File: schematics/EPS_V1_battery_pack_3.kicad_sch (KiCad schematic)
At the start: 31 parts, among them U10 MP2672AGD-0000-Z, U11 MAX17205G+

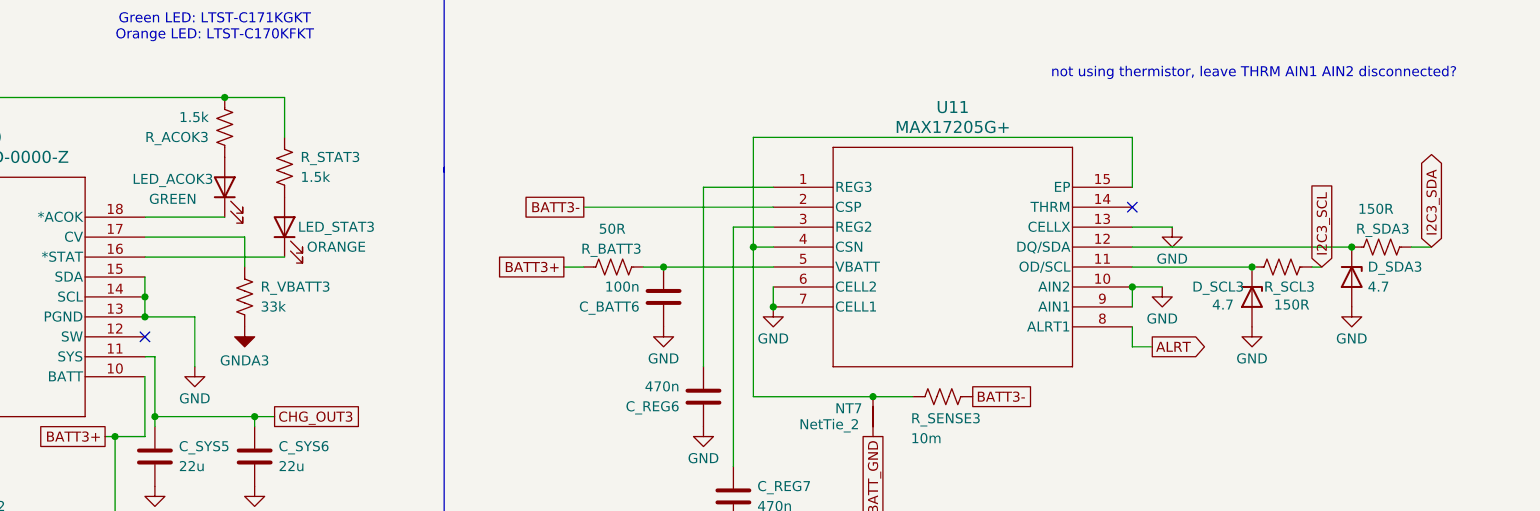
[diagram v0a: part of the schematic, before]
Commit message: Add chargers to I2C, chg_in for ADC
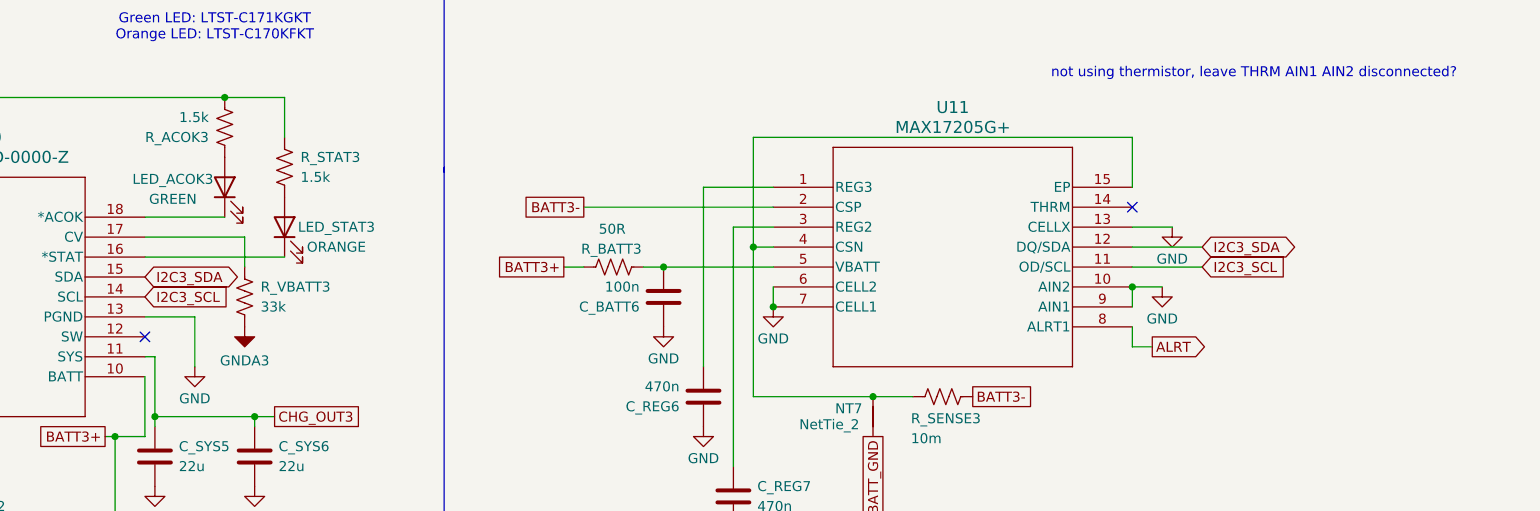
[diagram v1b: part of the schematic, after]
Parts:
- removed D_SCL3, D_SDA3: 4.7, Diode_SMD:D_0603_1608Metric, symbol Device:D_Zener
- removed R_SCL3, R_SDA3: 150R, Resistor_SMD:R_0603_1608Metric, symbol Device:R_US
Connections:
- net GND: no longer U10.14 (SCL), U10.15 (SDA)
- net I2C3_SCL: now also U10.14 (SCL), U11.11 (OD/SCL)
- net I2C3_SDA: now also U10.15 (SDA), U11.12 (DQ/SDA)

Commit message: Fix standalone to host control mode
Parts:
- removed R_VBATT3: 33k, Resistor_SMD:R_0603_1608Metric, symbol Device:R_US
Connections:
- net at C_VCC3.2, R_ACOK3.2, R_STAT3.1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: now also U10.17 (CV)
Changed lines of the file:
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@@
+	)
+	(junction
+		(at 105.41 63.5)
+		(diameter 0)
+		(color 0 0 0 0)
 	)
 	(junction
@@
 		)
 	)
-	(wire
-		(pts
-			(xy 104.14 81.28) (xy 116.84 81.28)
-		)
-		(stroke
-			(width 0)
-			(type default)
-		)
-	)
 	(polyline
 		(pts
@@
 	(wire
 		(pts
-			(xy 114.3 63.5) (xy 48.26 63.5)
+			(xy 104.14 81.28) (xy 105.41 81.28)
+		)
+		(stroke
+			(width 0)
+			(type default)
+		)
+	)
+	(wire
+		(pts
+			(xy 114.3 63.5) (xy 105.41 63.5)
 		)
 		(stroke
@@
 	(wire
 		(pts
+			(xy 105.41 81.28) (xy 105.41 63.5)
+		)
+		(stroke
+			(width 0)
+			(type default)
+		)
+	)
+	(wire
+		(pts
+			(xy 105.41 63.5) (xy 48.26 63.5)
+		)
+		(stroke
+			(width 0)
+			(type default)
+		)
+	)
+	(wire
+		(pts
 			(xy 45.72 91.44) (xy 45.72 106.68)
 		)
@@
 		(pts
 			(xy 104.14 106.68) (xy 104.14 99.06)
-		)
-		(stroke
-			(width 0)
-			(type default)
-		)
-	)
-	(wire
-		(pts
-			(xy 116.84 81.28) (xy 116.84 85.09)
 		)
 		(stroke
@@
 				(path "/85157432-5d03-48fa-ab40-27ed3d133f47/eb164b0c-5007-4f8f-b822-af0e1d9e197d"
 					(reference "#PWR0101")
-					(unit 1)
-				)
-			)
-		)
-	)
-	(symbol
-		(lib_id "sym_lib:GNDA3")
-		(at 116.84 92.71 0)
-		(unit 1)
-		(body_style 1)
-		(exclude_from_sim no)
-		(in_bom yes)
-		(on_board yes)
-		(in_pos_files yes)
-		(dnp no)
-		(property "Reference" "#PWR075"
-			(at 116.84 92.71 0)
-			(hide yes)
-			(show_name no)
-			(do_not_autoplace no)
-			(effects
-				(font
-					(size 1.27 1.27)
-				)
-			)
-		)
-		(property "Value" "GNDA3"
-			(at 116.84 97.028 0)
-			(show_name no)
-			(do_not_autoplace no)
-			(effects
-				(font
-					(size 1.27 1.27)
-				)
-			)
-		)
-		(property "Footprint" ""
-			(at 116.84 92.71 0)
-			(hide yes)
-			(show_name no)
-			(do_not_autoplace no)
-			(effects
-				(font
-					(size 1.27 1.27)
-				)
-			)
-		)
-		(property "Datasheet" ""
-			(at 116.84 92.71 0)
-			(hide yes)
-			(show_name no)
-			(do_not_autoplace no)
-			(effects
-				(font
-					(size 1.27 1.27)
-				)
-			)
-		)
-		(property "Description" ""
-			(at 116.84 92.71 0)
-			(hide yes)
-			(show_name no)
-			(do_not_autoplace no)
-			(effects
-				(font
-					(size 1.27 1.27)
-				)
-			)
-		)
-		(pin "1"
-		)
-		(instances
-			(project "EPS_V1"
-				(path "/85157432-5d03-48fa-ab40-27ed3d133f47/eb164b0c-5007-4f8f-b822-af0e1d9e197d"
-					(reference "#PWR075")
 					(unit 1)
 				)
@@
 					(unit 1)
 				)
-			)
-		)
-	)
-	(symbol
-		(lib_id "Device:R_US")
-		(at 116.84 88.9 0)
-		(unit 1)
-		(body_style 1)
-		(exclude_from_sim no)
-		(in_bom yes)
-		(on_board yes)
-		(in_pos_files yes)
-		(dnp no)
-		(property "Reference" "R_VBATT3"
-			(at 118.872 87.63 0)
-			(show_name no)
-			(do_not_autoplace no)
-			(effects
-				(font
-					(size 1.27 1.27)
-				)
-				(justify left)
-			)
-		)
-		(property "Value" "33k"
-			(at 118.872 90.17 0)
-			(show_name no)
-			(do_not_autoplace no)
-			(effects
-				(font
-					(size 1.27 1.27)
-				)
-				(justify left)
-			)
-		)
-		(property "Footprint" "Resistor_SMD:R_0603_1608Metric"
-			(at 117.856 89.154 90)
-			(hide yes)
-			(show_name no)
-			(do_not_autoplace no)
-			(effects
-				(font
-					(size 1.27 1.27)
-				)
-			)
-		)
-		(property "Datasheet" ""
-			(at 116.84 88.9 0)
-			(hide yes)
-			(show_name no)
-			(do_not_autoplace no)
-			(effects
-				(font
-					(size 1.27 1.27)
-				)
-			)
-		)
-		(property "Description" "Resistor, US symbol"
-			(at 116.84 88.9 0)
-			(hide yes)
-			(show_name no)
-			(do_not_autoplace no)
-			(effects
-				(font
-					(size 1.27 1.27)
-				)
-			)
-		)
-		(pin "2"
-		)
-		(pin "1"
-		)
-		(instances
-			(project "EPS_V1"
-				(path "/85157432-5d03-48fa-ab40-27ed3d133f47/eb164b0c-5007-4f8f-b822-af0e1d9e197d"
-					(reference "R_VBATT3")
-					(unit 1)
-				)
